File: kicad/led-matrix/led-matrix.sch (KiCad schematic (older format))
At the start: 14 parts, among them J1 INPUT_CONN, J2 OUTPUT_CONN, U1 74HCT4051, U2 MIC2981_82YN, U3 TPIC6C595N

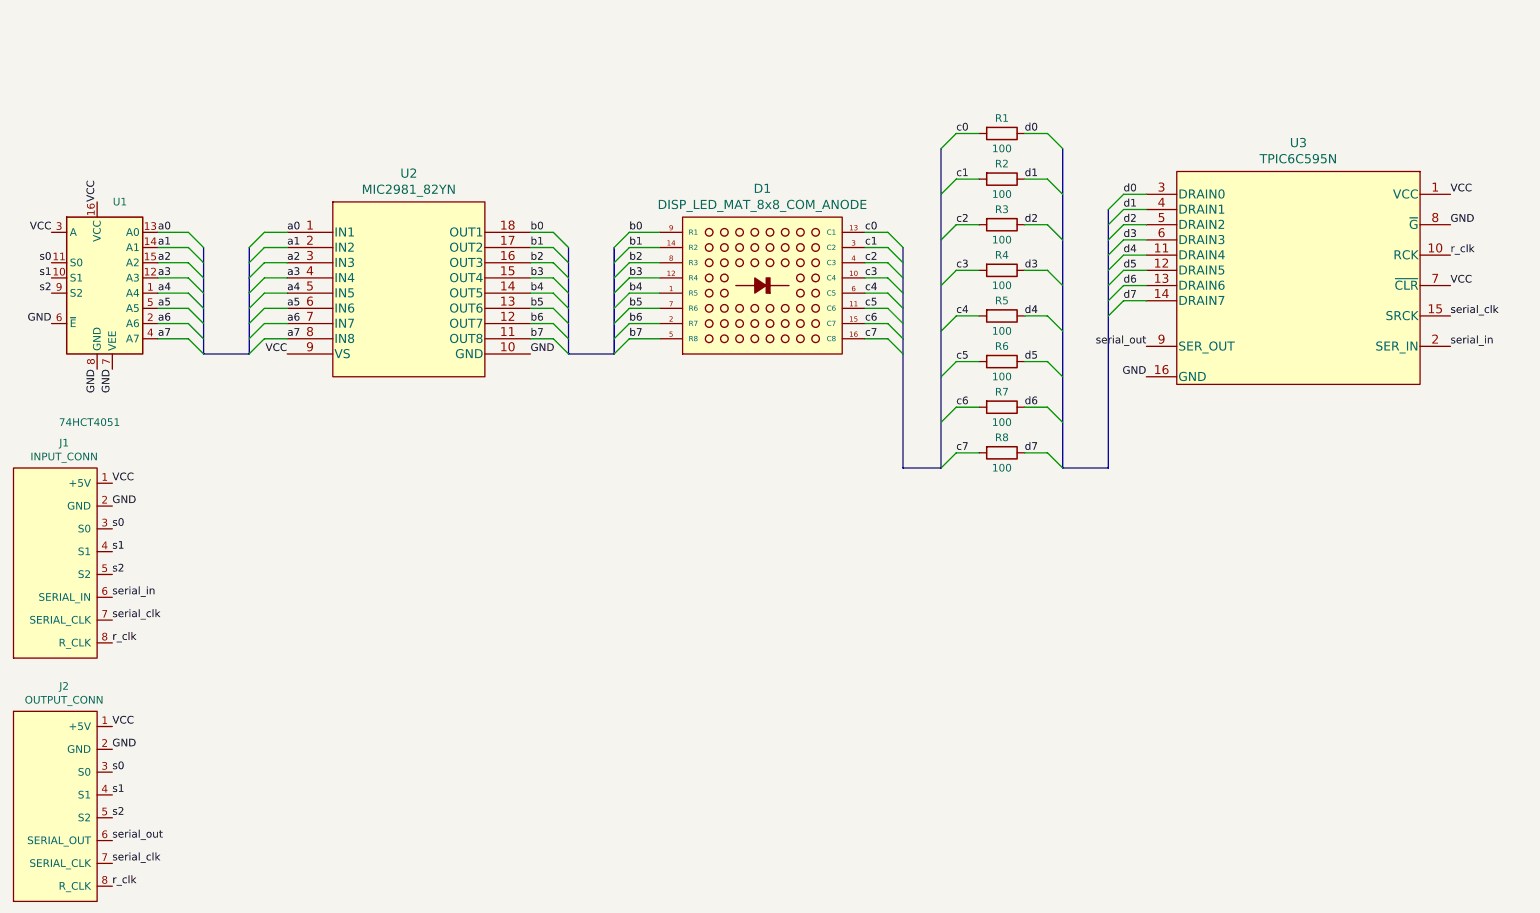
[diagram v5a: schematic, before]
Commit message: Kicad: Schematic: Add capacitors and additional resistor
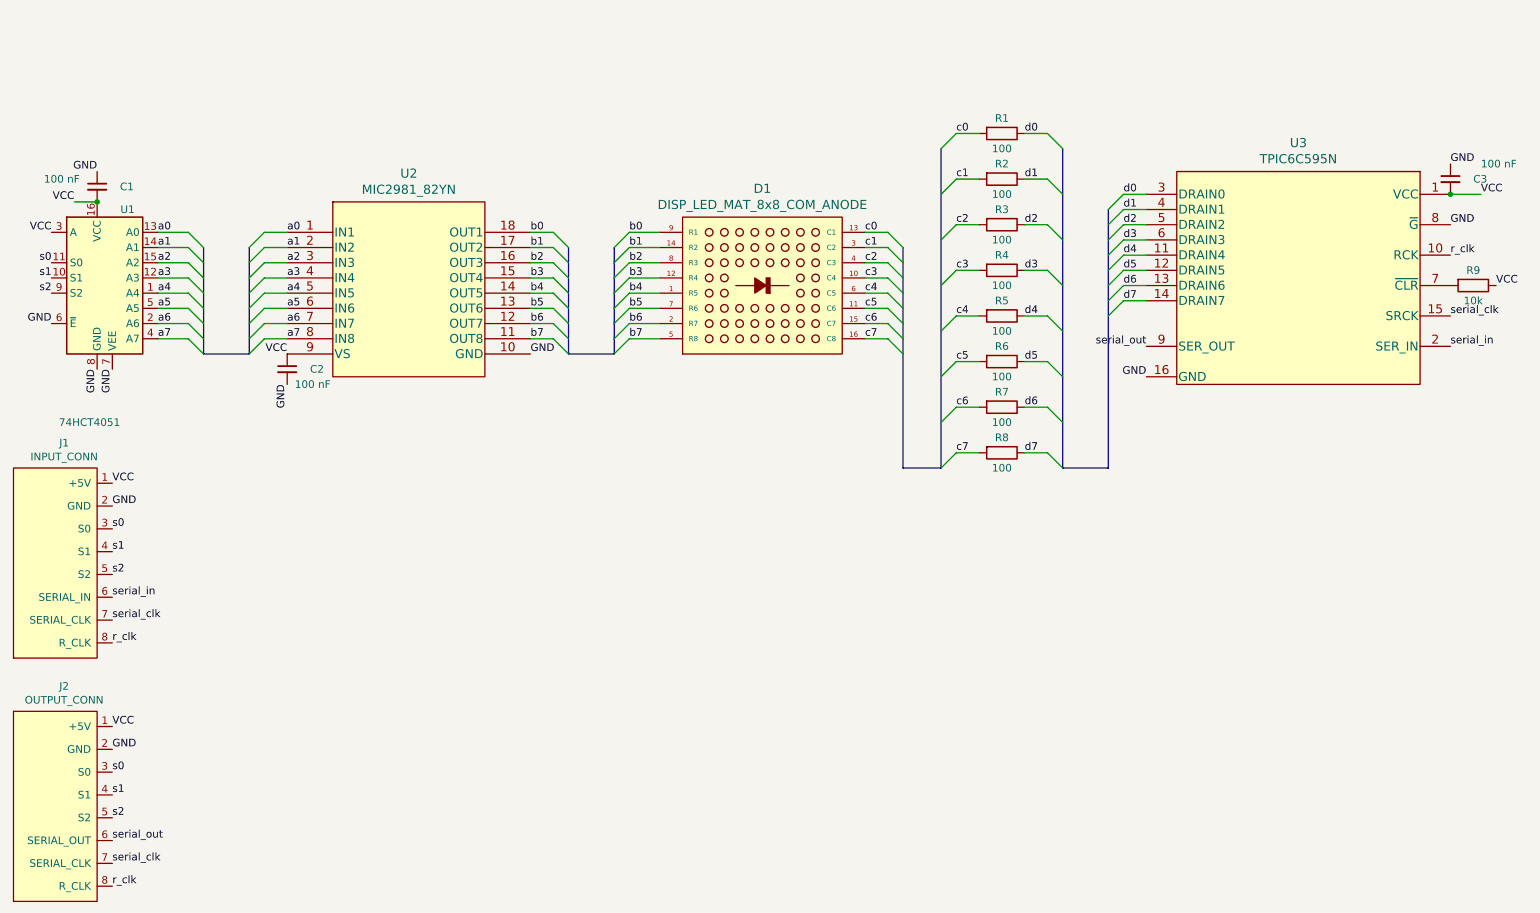
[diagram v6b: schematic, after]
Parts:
- added C1, C2, C3: 100 nF, Capacitor_SMD:C_1206_3216Metric_Pad1.33x1.80mm_HandSolder, symbol Device:C_Small
- added R9: 10k, Resistor_SMD:R_1206_3216Metric_Pad1.30x1.75mm_HandSolder, symbol Device:R
- R1, R2, R3, R4, R5, R6, R7, R8: footprint Resistor_SMD:R_0603_1608Metric_Pad0.98x0.95mm_HandSolder -> Resistor_SMD:R_1206_3216Metric_Pad1.30x1.75mm_HandSolder
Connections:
- net GND: now also C1.1, C2.2, C3.1
- net VCC: now also C1.2, C2.1, C3.2, R9.1; no longer U3.7 (~CLR)
- new net: R9.2, U3.7 (~CLR)
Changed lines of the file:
@@
 Entry Wire Line
 	1950 2500 2050 2600
-Text Label 1350 1600 1    50   ~ 0
+Text Label 1200 1600 2    50   ~ 0
 VCC
 Text Label 2600 2600 2    50   ~ 0
@@
 	-1   0    0    -1
 $EndComp
-Text Label 10250 1550 0    50   ~ 0
-VCC
-Text Label 10250 2150 0    50   ~ 0
+Text Label 10450 1550 0    50   ~ 0
+VCC
+Text Label 10550 2150 0    50   ~ 0
 VCC
 Text Label 1350 2700 3    50   ~ 0
-GND
-Text Label 1450 2700 3    50   ~ 0
 GND
 Text Label 4200 2600 0    50   ~ 0
@@
 F 0 "R3" V 7200 1750 50  0000 C CNN
 F 1 "100" V 7400 1750 50  0000 C CNN
-F 2 "Resistor_SMD:R_0603_1608Metric_Pad0.98x0.95mm_HandSolder" V 7230 1750 50  0001 C CNN
+F 2 "Resistor_SMD:R_1206_3216Metric_Pad1.30x1.75mm_HandSolder" V 7230 1750 50  0001 C CNN
 F 3 "~" H 7300 1750 50  0001 C CNN
 	1    7300 1750
@@
 F 0 "R4" V 7200 2050 50  0000 C CNN
 F 1 "100" V 7400 2050 50  0000 C CNN
-F 2 "Resistor_SMD:R_0603_1608Metric_Pad0.98x0.95mm_HandSolder" V 7230 2050 50  0001 C CNN
+F 2 "Resistor_SMD:R_1206_3216Metric_Pad1.30x1.75mm_HandSolder" V 7230 2050 50  0001 C CNN
 F 3 "~" H 7300 2050 50  0001 C CNN
 	1    7300 2050
@@
 F 0 "R5" V 7200 2350 50  0000 C CNN
 F 1 "100" V 7400 2350 50  0000 C CNN
-F 2 "Resistor_SMD:R_0603_1608Metric_Pad0.98x0.95mm_HandSolder" V 7230 2350 50  0001 C CNN
+F 2 "Resistor_SMD:R_1206_3216Metric_Pad1.30x1.75mm_HandSolder" V 7230 2350 50  0001 C CNN
 F 3 "~" H 7300 2350 50  0001 C CNN
 	1    7300 2350
@@
 F 0 "R6" V 7200 2650 50  0000 C CNN
 F 1 "100" V 7400 2650 50  0000 C CNN
-F 2 "Resistor_SMD:R_0603_1608Metric_Pad0.98x0.95mm_HandSolder" V 7230 2650 50  0001 C CNN
+F 2 "Resistor_SMD:R_1206_3216Metric_Pad1.30x1.75mm_HandSolder" V 7230 2650 50  0001 C CNN
 F 3 "~" H 7300 2650 50  0001 C CNN
 	1    7300 2650
@@
 F 0 "R7" V 7200 2950 50  0000 C CNN
 F 1 "100" V 7400 2950 50  0000 C CNN
-F 2 "Resistor_SMD:R_0603_1608Metric_Pad0.98x0.95mm_HandSolder" V 7230 2950 50  0001 C CNN
+F 2 "Resistor_SMD:R_1206_3216Metric_Pad1.30x1.75mm_HandSolder" V 7230 2950 50  0001 C CNN
 F 3 "~" H 7300 2950 50  0001 C CNN
 	1    7300 2950
@@
 F 0 "R2" V 7200 1450 50  0000 C CNN
 F 1 "100" V 7400 1450 50  0000 C CNN
-F 2 "Resistor_SMD:R_0603_1608Metric_Pad0.98x0.95mm_HandSolder" V 7230 1450 50  0001 C CNN
+F 2 "Resistor_SMD:R_1206_3216Metric_Pad1.30x1.75mm_HandSolder" V 7230 1450 50  0001 C CNN
 F 3 "~" H 7300 1450 50  0001 C CNN
 	1    7300 1450
@@
 F 0 "R1" V 7200 1150 50  0000 C CNN
 F 1 "100" V 7400 1150 50  0000 C CNN
-F 2 "Resistor_SMD:R_0603_1608Metric_Pad0.98x0.95mm_HandSolder" V 7230 1150 50  0001 C CNN
+F 2 "Resistor_SMD:R_1206_3216Metric_Pad1.30x1.75mm_HandSolder" V 7230 1150 50  0001 C CNN
 F 3 "~" H 7300 1150 50  0001 C CNN
 	1    7300 1150
@@
 Text Label 1450 3600 0    50   ~ 0
 GND
-Text Label 1050 1800 2    50   ~ 0
-VCC
 $Comp
 L 74xx:74HCT4051 U1
 U 1 1 5FD7E6DB
 P 1350 2100
-F 0 "U1" H 1500 2600 50  0000 C CNN
+F 0 "U1" H 1550 2550 50  0000 C CNN
 F 1 "74HCT4051" H 1300 1150 50  0000 C CNN
 F 2 "Package_DIP:DIP-16_W7.62mm" H 1350 1700 50  0001 C CNN
@@
 F 0 "R8" V 7200 3250 50  0000 C CNN
 F 1 "100" V 7400 3250 50  0000 C CNN
-F 2 "Resistor_SMD:R_0603_1608Metric_Pad0.98x0.95mm_HandSolder" V 7230 3250 50  0001 C CNN
+F 2 "Resistor_SMD:R_1206_3216Metric_Pad1.30x1.75mm_HandSolder" V 7230 3250 50  0001 C CNN
 F 3 "~" H 7300 3250 50  0001 C CNN
 	1    7300 3250
@@
 Text Label 1450 3450 0    50   ~ 0
 VCC
+$Comp
+L Device:R R9
+U 1 1 5FE2FB77
+P 10400 2150
+F 0 "R9" V 10300 2150 50  0000 C CNN
+F 1 "10k" V 10500 2150 50  0000 C CNN
+F 2 "Resistor_SMD:R_1206_3216Metric_Pad1.30x1.75mm_HandSolder" V 10330 2150 50  0001 C CNN
+F 3 "~" H 10400 2150 50  0001 C CNN
+	1    10400 2150
+	0    1    1    0
+$EndComp
+$Comp
+L Device:C_Small C1
+U 1 1 5FE506E1
+P 1350 1500
+F 0 "C1" H 1500 1500 50  0000 L CNN
+F 1 "100 nF" H 1000 1550 50  0000 L CNN
+F 2 "Capacitor_SMD:C_1206_3216Metric_Pad1.33x1.80mm_HandSolder" H 1350 1500 50  0001 C CNN
+F 3 "~" H 1350 1500 50  0001 C CNN
+	1    1350 1500
+	1    0    0    -1
+$EndComp
+Text Label 1050 1800 2    50   ~ 0
+VCC
+Wire Wire Line
+	1350 1600 1200 1600
+Connection ~ 1350 1600
+Text Label 1350 1400 2    50   ~ 0
+GND
+$Comp
+L Device:C_Small C2
+U 1 1 5FE5FD6A
+P 2600 2700
+F 0 "C2" H 2750 2700 50  0000 L CNN
+F 1 "100 nF" H 2650 2600 50  0000 L CNN
+F 2 "Capacitor_SMD:C_1206_3216Metric_Pad1.33x1.80mm_HandSolder" H 2600 2700 50  0001 C CNN
+F 3 "~" H 2600 2700 50  0001 C CNN
+	1    2600 2700
+	1    0    0    -1
+$EndComp
+Text Label 2600 2800 3    50   ~ 0
+GND
+$Comp
+L Device:C_Small C3
+U 1 1 5FE60FA7
+P 10250 1450
+F 0 "C3" H 10400 1450 50  0000 L CNN
+F 1 "100 nF" H 10450 1550 50  0000 L CNN
+F 2 "Capacitor_SMD:C_1206_3216Metric_Pad1.33x1.80mm_HandSolder" H 10250 1450 50  0001 C CNN
+F 3 "~" H 10250 1450 50  0001 C CNN
+	1    10250 1450
+	1    0    0    -1
+$EndComp
+Text Label 10250 1350 0    50   ~ 0
+GND
+Wire Wire Line
+	10250 1550 10450 1550
+Connection ~ 10250 1550
+Text Label 1450 2700 3    50   ~ 0
+GND
 Wire Bus Line
 	4750 1900 4750 2600

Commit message: Updated 3D model and fixed Edge.Cuts layer
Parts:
- D1: footprint akn_misc:LED_8x8_3MM_32x32MM -> led_matrix:LED_8x8_7.62MM_60.2x60.2MM
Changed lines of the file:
@@
 F 0 "D1" H 5725 3687 60  0000 C CNN
 F 1 "DISP_LED_MAT_8x8_COM_ANODE" H 5725 3581 60  0000 C CNN
-F 2 "akn_misc:LED_8x8_3MM_32x32MM" H 5150 2550 60  0001 C CNN
+F 2 "led_matrix:LED_8x8_7.62MM_60.2x60.2MM" H 5150 2550 60  0001 C CNN
 F 3 "" H 5150 2550 60  0000 C CNN
 	1    5050 2600

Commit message: KiCad: Schematic: Update footprint for J1 and J2
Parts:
- J1: footprint Connector_PinHeader_2.00mm:PinHeader_1x08_P2.00mm_Vertical -> Connector_PinSocket_2.54mm:PinSocket_1x08_P2.54mm_Horizontal
- J2: footprint Connector_PinHeader_2.00mm:PinHeader_1x08_P2.00mm_Vertical -> Connector_PinHeader_2.54mm:PinHeader_1x08_P2.54mm_Horizontal
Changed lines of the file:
@@
 F 0 "J1" H 1133 3415 50  0000 C CNN
 F 1 "INPUT_CONN" H 1133 3324 50  0000 C CNN
-F 2 "Connector_PinHeader_2.00mm:PinHeader_1x08_P2.00mm_Vertical" H 1450 3300 50  0001 C CNN
+F 2 "Connector_PinSocket_2.54mm:PinSocket_1x08_P2.54mm_Horizontal" H 1450 3300 50  0001 C CNN
 F 3 "" H 1450 3300 50  0001 C CNN
 	1    1450 3300
@@
 F 0 "J2" H 1133 5015 50  0000 C CNN
 F 1 "OUTPUT_CONN" H 1133 4924 50  0000 C CNN
-F 2 "Connector_PinHeader_2.00mm:PinHeader_1x08_P2.00mm_Vertical" H 1450 4900 50  0001 C CNN
+F 2 "Connector_PinHeader_2.54mm:PinHeader_1x08_P2.54mm_Horizontal" H 1450 4900 50  0001 C CNN
 F 3 "" H 1450 4900 50  0001 C CNN
 	1    1450 4900
